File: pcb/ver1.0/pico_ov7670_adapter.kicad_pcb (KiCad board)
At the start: 2 copper layers, 49 x 56 mm, 26 parts, among them J1 GPIO Header, SW1 SW_Push, SW2 SW_Push, U1 CAMERA-OV7670, U2 RASPBERRY_PI_PICO_W

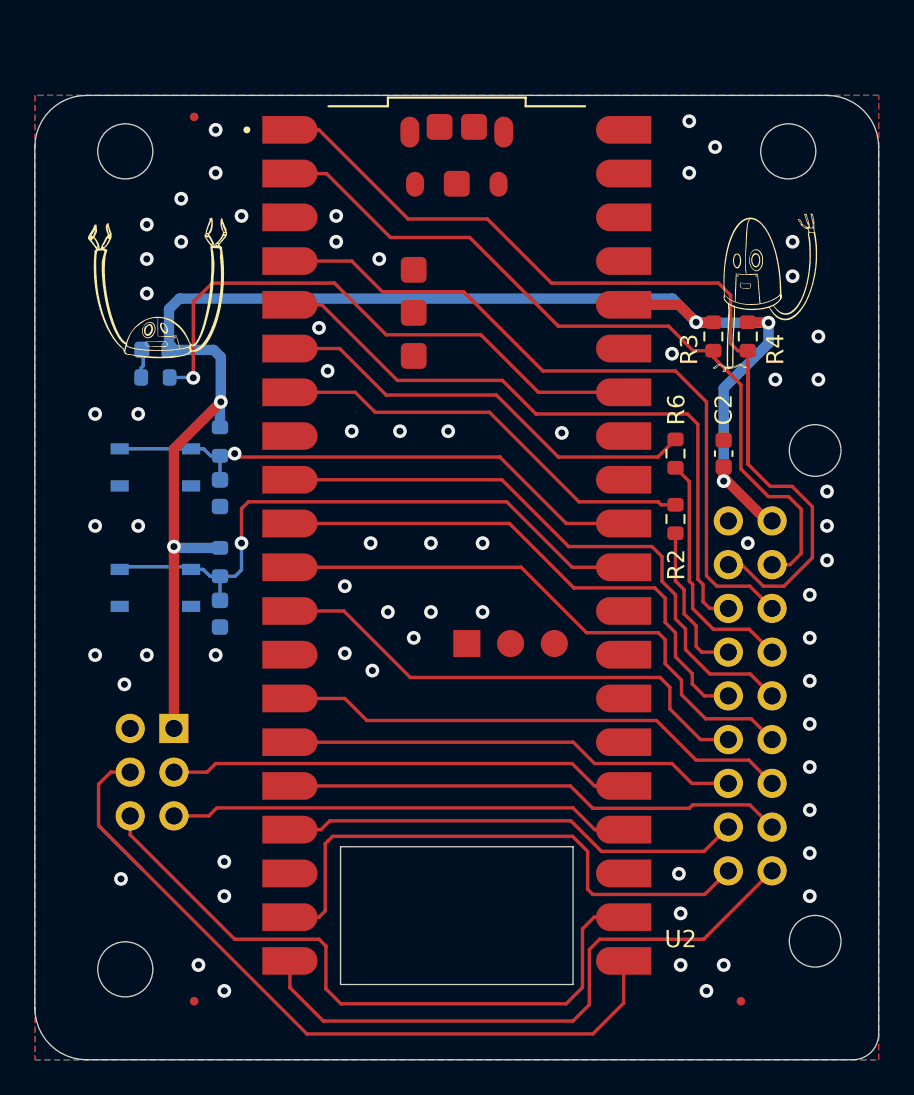
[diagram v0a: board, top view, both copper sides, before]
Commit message: camera module footptint updated.
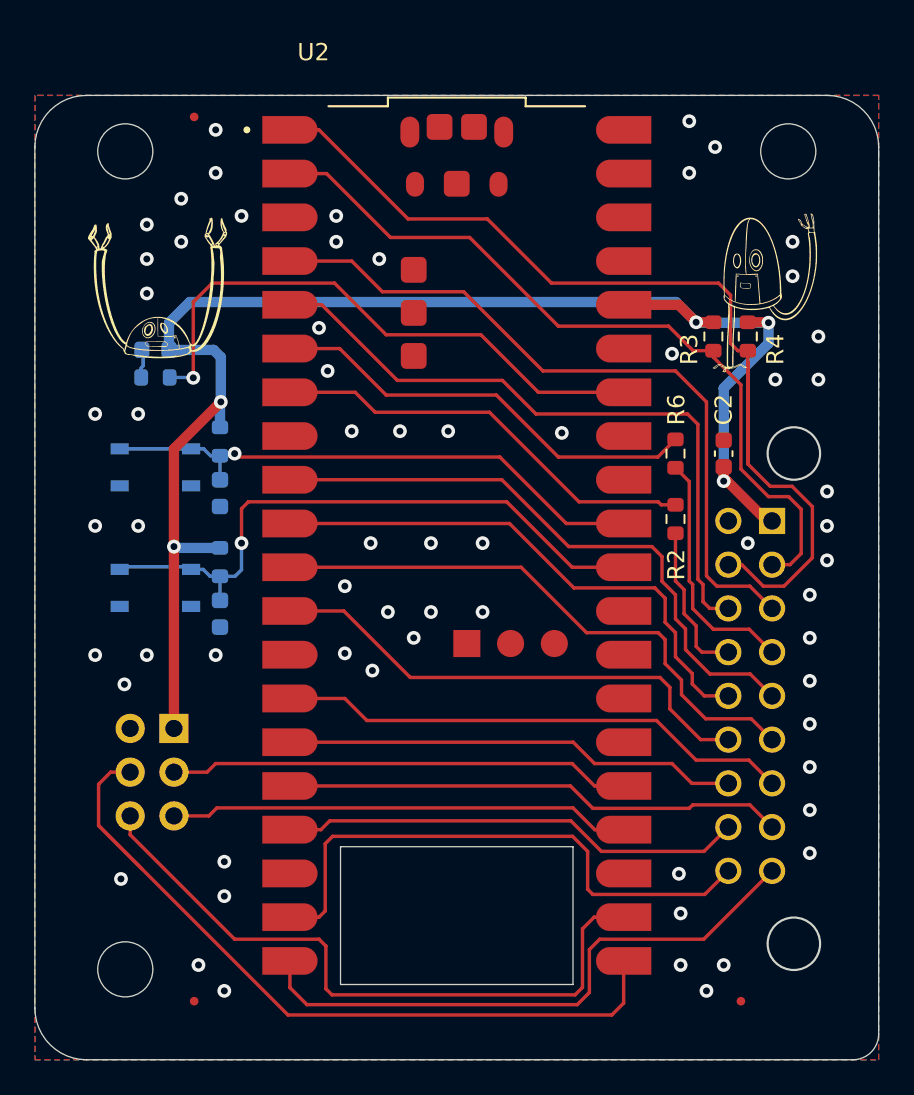
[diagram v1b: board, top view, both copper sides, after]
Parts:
- U1: footprint pico_ov7670_adapter:ov7670_camera module -> pico_ov7670_adapter:CAMERA-OV7670-DIP
- moved U1 12.2 mm to (117.3, 101.0)
- moved G*** 0.92 mm to (112.5, 75.0)
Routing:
- net OV_RST_PICO_IO15: track 35.8 -> 34.6 mm
- net /PICO_IO16: track 46.8 -> 45.8 mm
- net +3V3: track 89.8 -> 89.2 mm
- net GND: vias 66 -> 65
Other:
- board text added: "Ver 1.0"
- board text removed: "Ver 0.1"
